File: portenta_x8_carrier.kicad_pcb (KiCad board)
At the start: 2 copper layers, 2 parts, among them J1 4049_80pos_High_Density, J2 4049_80pos_High_Density

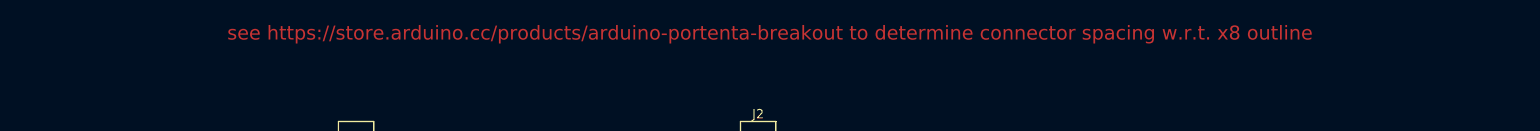
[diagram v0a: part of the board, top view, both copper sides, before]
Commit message: Got spacing of high-density connectors
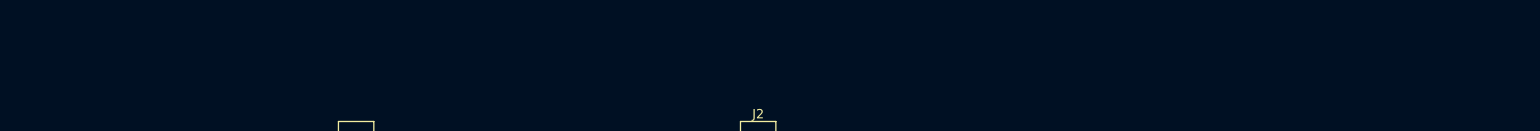
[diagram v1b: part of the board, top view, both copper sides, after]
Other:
- board text added: "Connector spacing determined by examining the STEP file of the board in Fusion 360. TODO -- follow up on GitHub issue"
- board text removed: "see https://store.arduino.cc/products/arduino-portenta-breakout to determine connector spacing w.r.t. x8 outline"
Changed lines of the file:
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@@
     )
   )
-  (gr_text "see https://store.arduino.cc/products/arduino-portenta-breakout to determine connector spacing w.r.t. x8 outline" (at 111.76 83.566) (layer "F.Cu")
+  (gr_line (start 114.173 89.662) (end 52.197 89.662) (layer "Dwgs.User") (width 0.15))
+  (gr_arc (start 116.205 113.03) (mid 115.609841 114.466841) (end 114.173 115.062) (layer "Dwgs.User") (width 0.15))
+  (gr_line (start 114.173 115.062) (end 52.197 115.062) (layer "Dwgs.User") (width 0.15))
+  (gr_arc (start 50.165 91.694) (mid 50.760159 90.257159) (end 52.197 89.662) (layer "Dwgs.User") (width 0.15))
+  (gr_arc (start 52.197 115.062) (mid 50.760159 114.466841) (end 50.165 113.03) (layer "Dwgs.User") (width 0.15))
+  (gr_arc (start 114.173 89.662) (mid 115.609841 90.257159) (end 116.205 91.694) (layer "Dwgs.User") (width 0.15))
+  (gr_line (start 50.165 91.694) (end 50.165 113.03) (layer "Dwgs.User") (width 0.15))
+  (gr_line (start 116.205 91.694) (end 116.205 113.03) (layer "Dwgs.User") (width 0.15))
+  (gr_text "Connector spacing determined by examining the STEP file\nof the board in Fusion 360. TODO -- follow up on GitHub issue" (at 62.23 132.461) (layer "Dwgs.User")
     (effects (font (size 1.5 1.5) (thickness 0.3)))
   )
+  (dimension (type orthogonal) (layer "Dwgs.User")
+    (pts (xy 114.173 115.062) (xy 114.046 89.662))
+    (height 7.366)
+    (orientation 1)
+    (gr_text "1000.0000 mils" (at 120.389 102.362 90) (layer "Dwgs.User")
+      (effects (font (size 1 1) (thickness 0.15)))
+    )
+    (format (units 3) (units_format 1) (precision 4))
+    (style (thickness 0.15) (arrow_length 1.27) (text_position_mode 0) (extension_height 0.58642) (extension_offset 0.5) keep_text_aligned)
+  )
+  (dimension (type orthogonal) (layer "Dwgs.User")
+    (pts (xy 110.49 102.362) (xy 67.31 102.362))
+    (height 16.51)
+    (orientation 0)
+    (gr_text "1700.0000 mils" (at 88.9 117.722) (layer "Dwgs.User")
+      (effects (font (size 1 1) (thickness 0.15)))
+    )
+    (format (units 3) (units_format 1) (precision 4))
+    (style (thickness 0.15) (arrow_length 1.27) (text_position_mode 0) (extension_height 0.58642) (extension_offset 0.5) keep_text_aligned)
+  )
+  (dimension (type orthogonal) (layer "Dwgs.User")
+    (pts (xy 110.49 102.362) (xy 116.205 102.362))
+    (height -15.367)
+    (orientation 0)
+    (gr_text "225.0000 mils" (at 113.3475 85.845) (layer "Dwgs.User")
+      (effects (font (size 1 1) (thickness 0.15)))
+    )
+    (format (units 3) (units_format 1) (precision 4))
+    (style (thickness 0.15) (arrow_length 1.27) (text_position_mode 0) (extension_height 0.58642) (extension_offset 0.5) keep_text_aligned)
+  )
+  (dimension (type orthogonal) (layer "Dwgs.User")
+    (pts (xy 110.49 102.362) (xy 110.49 115.062))
+    (height -5.715)
+    (orientation 1)
+    (gr_text "500.0000 mils" (at 103.625 108.712 90) (layer "Dwgs.User")
+      (effects (font (size 1 1) (thickness 0.15)))
+    )
+    (format (units 3) (units_format 1) (precision 4))
+    (style (thickness 0.15) (arrow_length 1.27) (text_position_mode 0) (extension_height 0.58642) (extension_offset 0.5) keep_text_aligned)
+  )
+  (dimension (type orthogonal) (layer "Dwgs.User")
+    (pts (xy 50.165 113.03) (xy 116.205 113.03))
+    (height 9.144)
+    (orientation 0)
+    (gr_text "2600.0000 mils" (at 83.185 121.024) (layer "Dwgs.User")
+      (effects (font (size 1 1) (thickness 0.15)))
+    )
+    (format (units 3) (units_format 1) (precision 4))
+    (style (thickness 0.15) (arrow_length 1.27) (text_position_mode 0) (extension_height 0.58642) (extension_offset 0.5) keep_text_aligned)
+  )
+  (dimension (type orthogonal) (layer "Dwgs.User")
+    (pts (xy 67.31 102.362) (xy 50.165 102.362))
+    (height -15.367)
+    (orientation 0)
+    (gr_text "675.0000 mils" (at 58.7375 85.845) (layer "Dwgs.User")
+      (effects (font (size 1 1) (thickness 0.15)))
+    )
+    (format (units 3) (units_format 1) (precision 4))
+    (style (thickness 0.15) (arrow_length 1.27) (text_position_mode 0) (extension_height 0.58642) (extension_offset 0.5) keep_text_aligned)
+  )
 )

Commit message: Started naming pins
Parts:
- moved J2 59.4 mm to (55.9, 79.0), turned to 90 degrees
- moved J1 39.4 mm to (99.1, 79.0), turned to -90 degrees
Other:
- board outline added: 66 x 48.8 mm

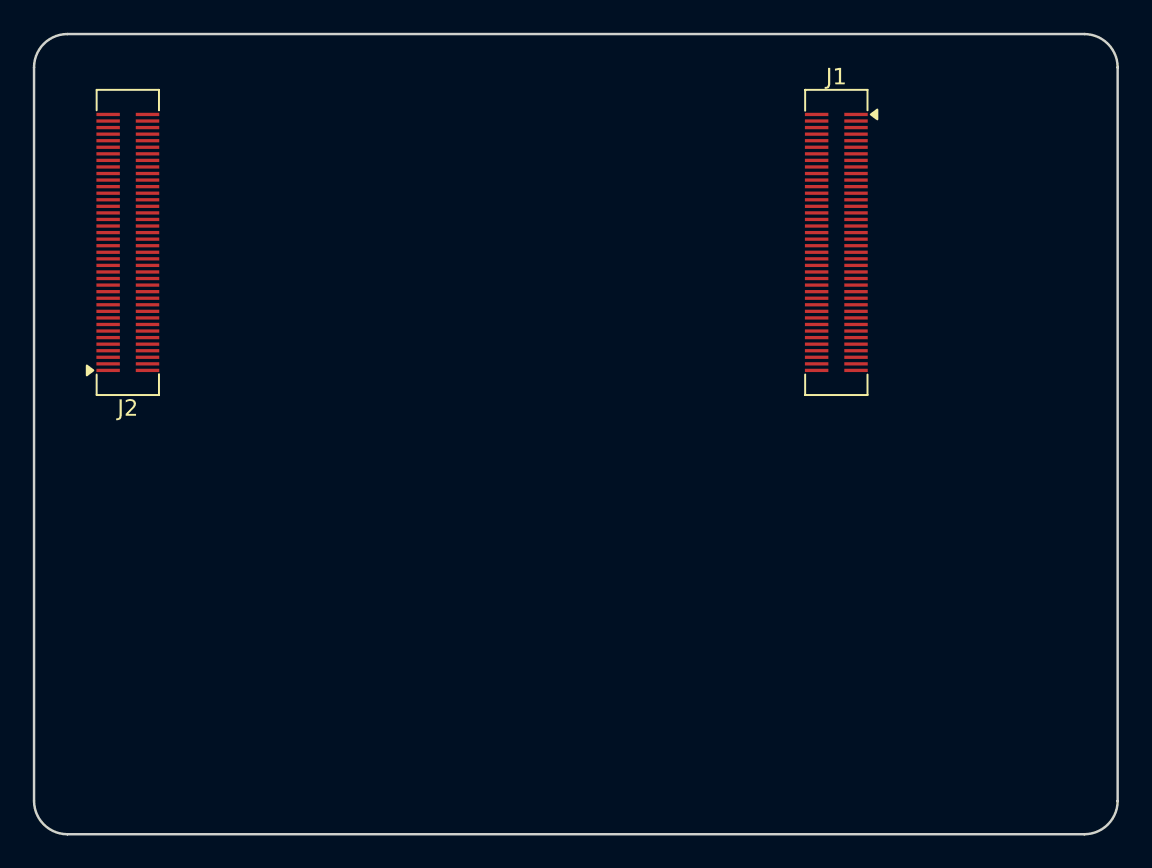
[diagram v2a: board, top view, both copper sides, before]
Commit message: Enhanced README, added license
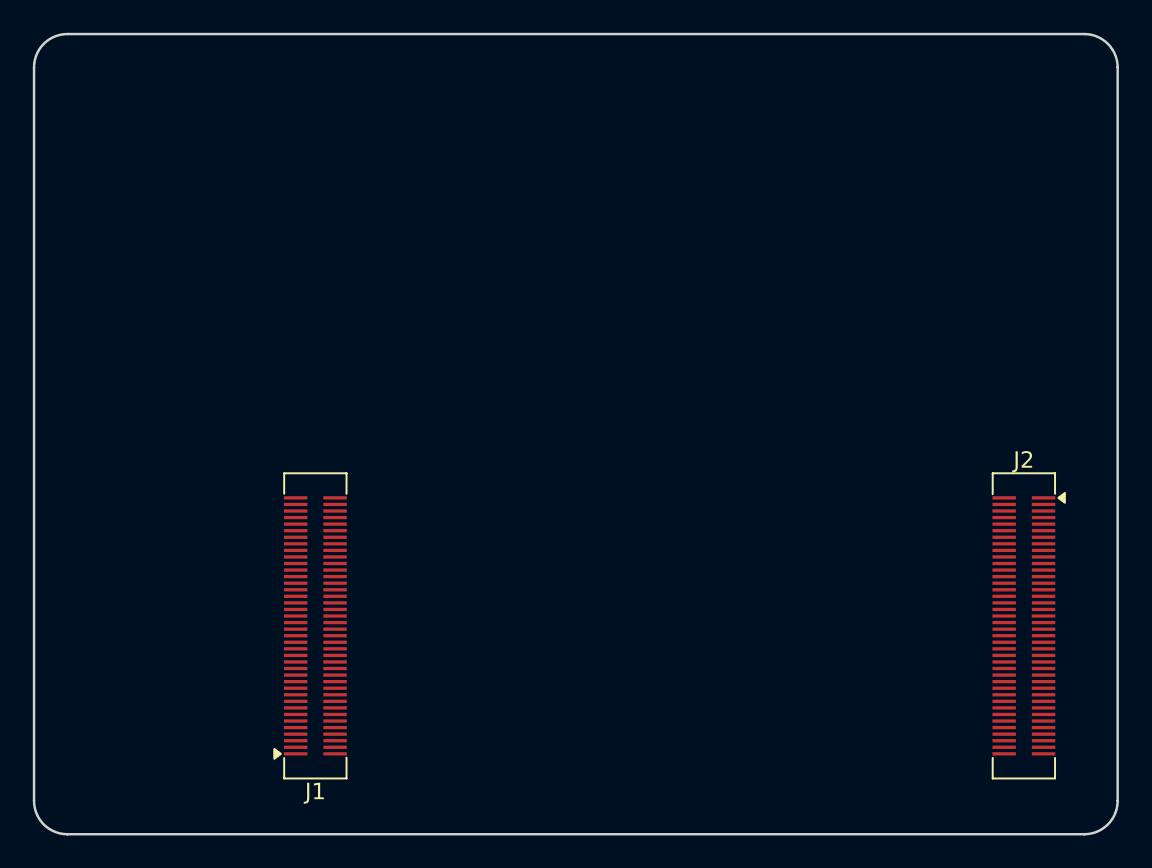
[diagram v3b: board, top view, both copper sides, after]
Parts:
- moved J2 59.4 mm to (110.5, 102.4), turned to -90 degrees
- moved J1 39.4 mm to (67.3, 102.4), turned to 90 degrees
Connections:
- J1 pad 1: unconnected-(J1-Pad1) -> /ETH_A+
- J1 pad 10: unconnected-(J1-Pad10) -> /MIPI_DSI_D1_P
- J1 pad 11: unconnected-(J1-Pad11) -> /ETH_C-
- J1 pad 12: unconnected-(J1-Pad12) -> /MIPI_DSI_D1_N
- J1 pad 13: unconnected-(J1-Pad13) -> /ETH_D+
- J1 pad 14: unconnected-(J1-Pad14) -> /MIPI_DSI_D0_P
- J1 pad 15: unconnected-(J1-Pad15) -> /ETH_D-
- J1 pad 16: unconnected-(J1-Pad16) -> /MIPI_DSI_D0_N
- J1 pad 17: unconnected-(J1-Pad17) -> /LED2_LINK
- J1 pad 18: unconnected-(J1-Pad18) -> /MIPI_DSI_CKL_P
- J1 pad 19: unconnected-(J1-Pad19) -> /LED2_ACT
- J1 pad 2: unconnected-(J1-Pad2) -> /MIPI_DSI_D3_P
- J1 pad 20: unconnected-(J1-Pad20) -> /MIPI_DSI_CKL_N
- J1 pad 21: unconnected-(J1-Pad21) -> /VSYS_5V
- J1 pad 22: unconnected-(J1-Pad22) -> GND
- J1 pad 23: unconnected-(J1-Pad23) -> /USB1_VBUS
- J1 pad 24: unconnected-(J1-Pad24) -> /USB2_VBUS
- J1 pad 25: unconnected-(J1-Pad25) -> /USB1_DP
- J1 pad 26: unconnected-(J1-Pad26) -> /USB2_DP
- J1 pad 27: unconnected-(J1-Pad27) -> /USB1_DN
- J1 pad 28: unconnected-(J1-Pad28) -> /USB2_DN
- J1 pad 29: unconnected-(J1-Pad29) -> /USB1_ID
- J1 pad 3: unconnected-(J1-Pad3) -> /ETH_A-
- J1 pad 30: unconnected-(J1-Pad30) -> /USB2_ID
- J1 pad 31: unconnected-(J1-Pad31) -> GND
- J1 pad 32: unconnected-(J1-Pad32) -> /VSYS_5V
- J1 pad 33: unconnected-(J1-Pad33) -> /UART2_TXD
- J1 pad 34: unconnected-(J1-Pad34) -> /UART_STM32_TXD
- J1 pad 35: unconnected-(J1-Pad35) -> /UART2_RXD
- J1 pad 36: unconnected-(J1-Pad36) -> /UART_STM32_RXD
- J1 pad 37: unconnected-(J1-Pad37) -> /UART2_RTS
- J1 pad 38: unconnected-(J1-Pad38) -> /UART_STM32_RTS
- J1 pad 39: unconnected-(J1-Pad39) -> /UART2_CTS
- J1 pad 4: unconnected-(J1-Pad4) -> /MIPI_DSI_D3_N
- J1 pad 40: unconnected-(J1-Pad40) -> /UART_STM32_CTS
- J1 pad 41: unconnected-(J1-Pad41) -> /VSYS_5V
- J1 pad 42: unconnected-(J1-Pad42) -> GND
- J1 pad 43: unconnected-(J1-Pad43) -> /I2C2_SDA
- J1 pad 44: unconnected-(J1-Pad44) -> /I2C3_SDA
- J1 pad 45: unconnected-(J1-Pad45) -> /I2C2_SCL
- J1 pad 46: unconnected-(J1-Pad46) -> /I2C3_SCL
- J1 pad 47: unconnected-(J1-Pad47) -> GND
- J1 pad 48: unconnected-(J1-Pad48) -> /VSYS_5V
- J1 pad 49: unconnected-(J1-Pad49) -> /CAN1_TX
- J1 pad 5: unconnected-(J1-Pad5) -> /ETH_B+
- J1 pad 51: unconnected-(J1-Pad51) -> /CAN1_RX
- J1 pad 53: unconnected-(J1-Pad53) -> /VSYS_5V
- J1 pad 54: unconnected-(J1-Pad54) -> GND
- J1 pad 6: unconnected-(J1-Pad6) -> /MIPI_DSI_D2_P
- J1 pad 64: unconnected-(J1-Pad64) -> /VSYS_5V
- J1 pad 7: unconnected-(J1-Pad7) -> /ETH_B-
- J1 pad 8: unconnected-(J1-Pad8) -> /MIPI_DSI_D2_N
- J1 pad 9: unconnected-(J1-Pad9) -> /ETH_C+
